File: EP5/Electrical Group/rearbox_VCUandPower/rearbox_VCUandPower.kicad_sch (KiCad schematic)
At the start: 49 parts, among them J1 JTAG, J2 MSD-4-A, J20 GPS_UART, J3 USB_OTG, SW1 BOOT0, SW2 VBUS, SW3 NRST, U1 STM32H562VGTx, U2 USBLC6-2SC6, Y1 24MHz, Y2 32.768kHz

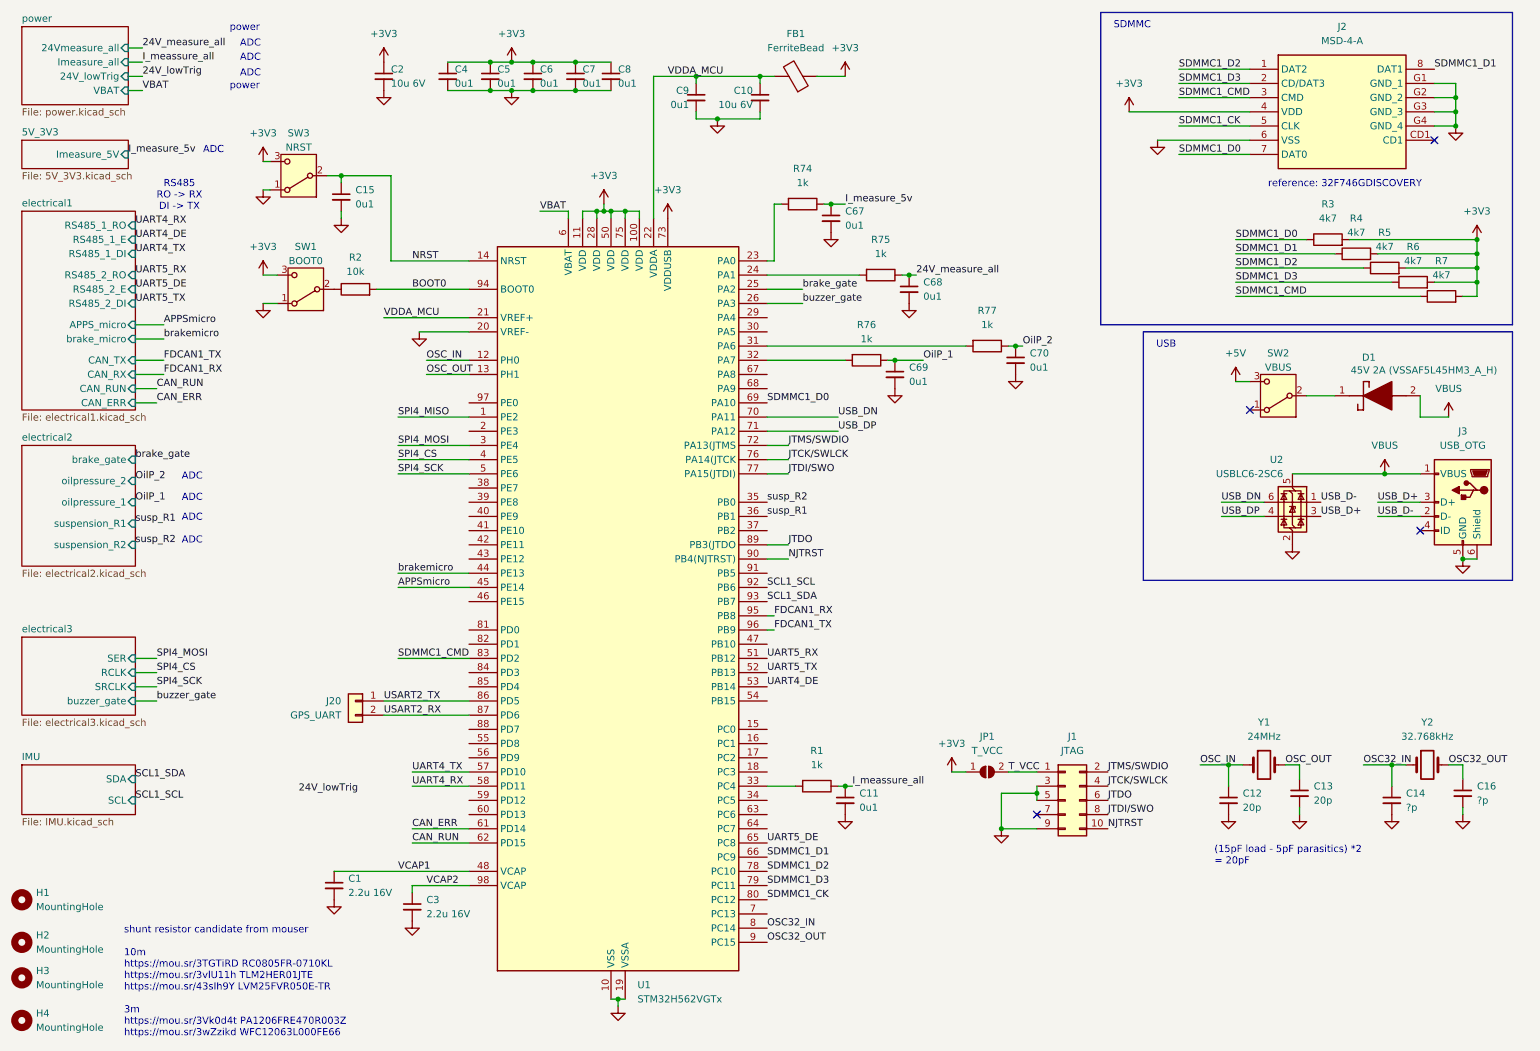
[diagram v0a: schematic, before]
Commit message: add rearbox_VCUandPower to EP5
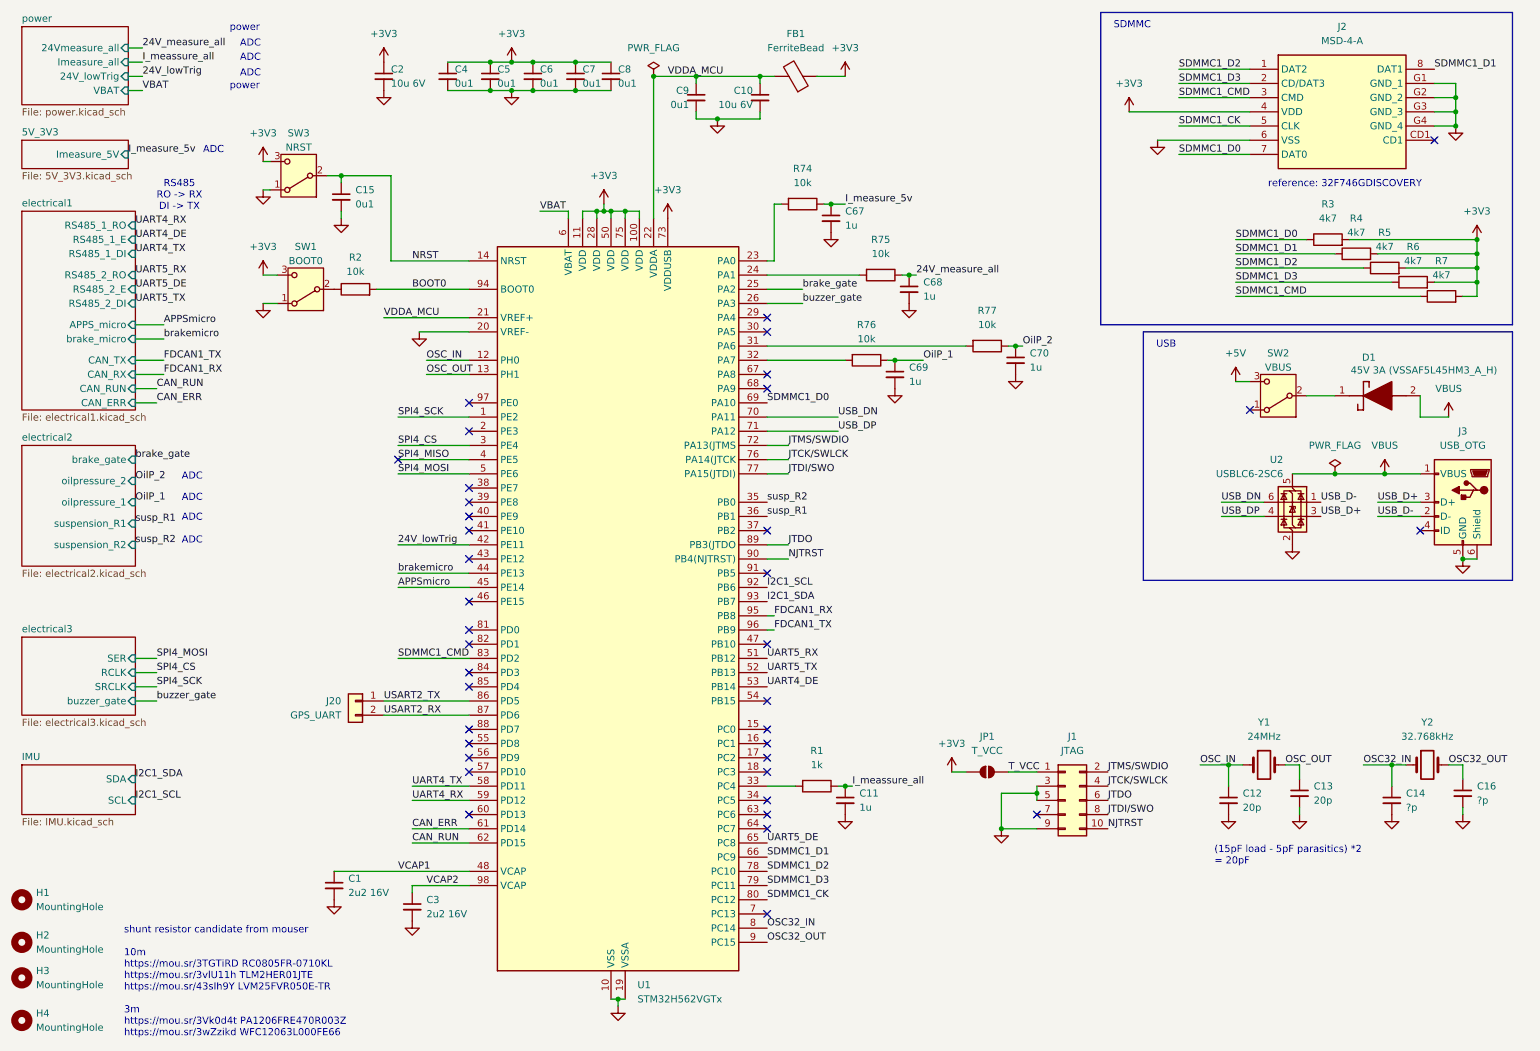
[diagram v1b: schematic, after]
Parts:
- C1, C3: value 2.2u 16V -> 2u2 16V
- C11, C67, C68, C69, C70: value 0u1 -> 1u
- D1: value 45V 2A (VSSAF5L45HM3_A_H) -> 45V 3A (VSSAF5L45HM3_A_H)
- R74, R75, R76, R77: value 1k -> 10k
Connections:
- net 24V_lowTrig: now also U1.42 (PE11)
- net SPI4_CS: now also U1.3 (PE4); no longer U1.4 (PE5)
- net SPI4_MISO: now also U1.4 (PE5); no longer U1.1 (PE2)
- net SPI4_MOSI: now also U1.5 (PE6); no longer U1.3 (PE4)
- net SPI4_SCK: now also U1.1 (PE2); no longer U1.5 (PE6)
- net UART4_RX: now also U1.59 (PD12); no longer U1.58 (PD11)
- net UART4_TX: now also U1.58 (PD11); no longer U1.57 (PD10)
- net SCL1_SCL renamed I2C1_SCL
- net SCL1_SDA renamed I2C1_SDA
- no-connect marks 4 -> 38
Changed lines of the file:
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@@
 		(rev "1.0")
 		(company "NTURacing")
-		(comment 1 "郭哲明")
+		(comment 1 "郭哲明 Jack Kuo")
 		(comment 2 "Electrical group")
 	)
